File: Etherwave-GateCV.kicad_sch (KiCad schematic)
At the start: 32 parts

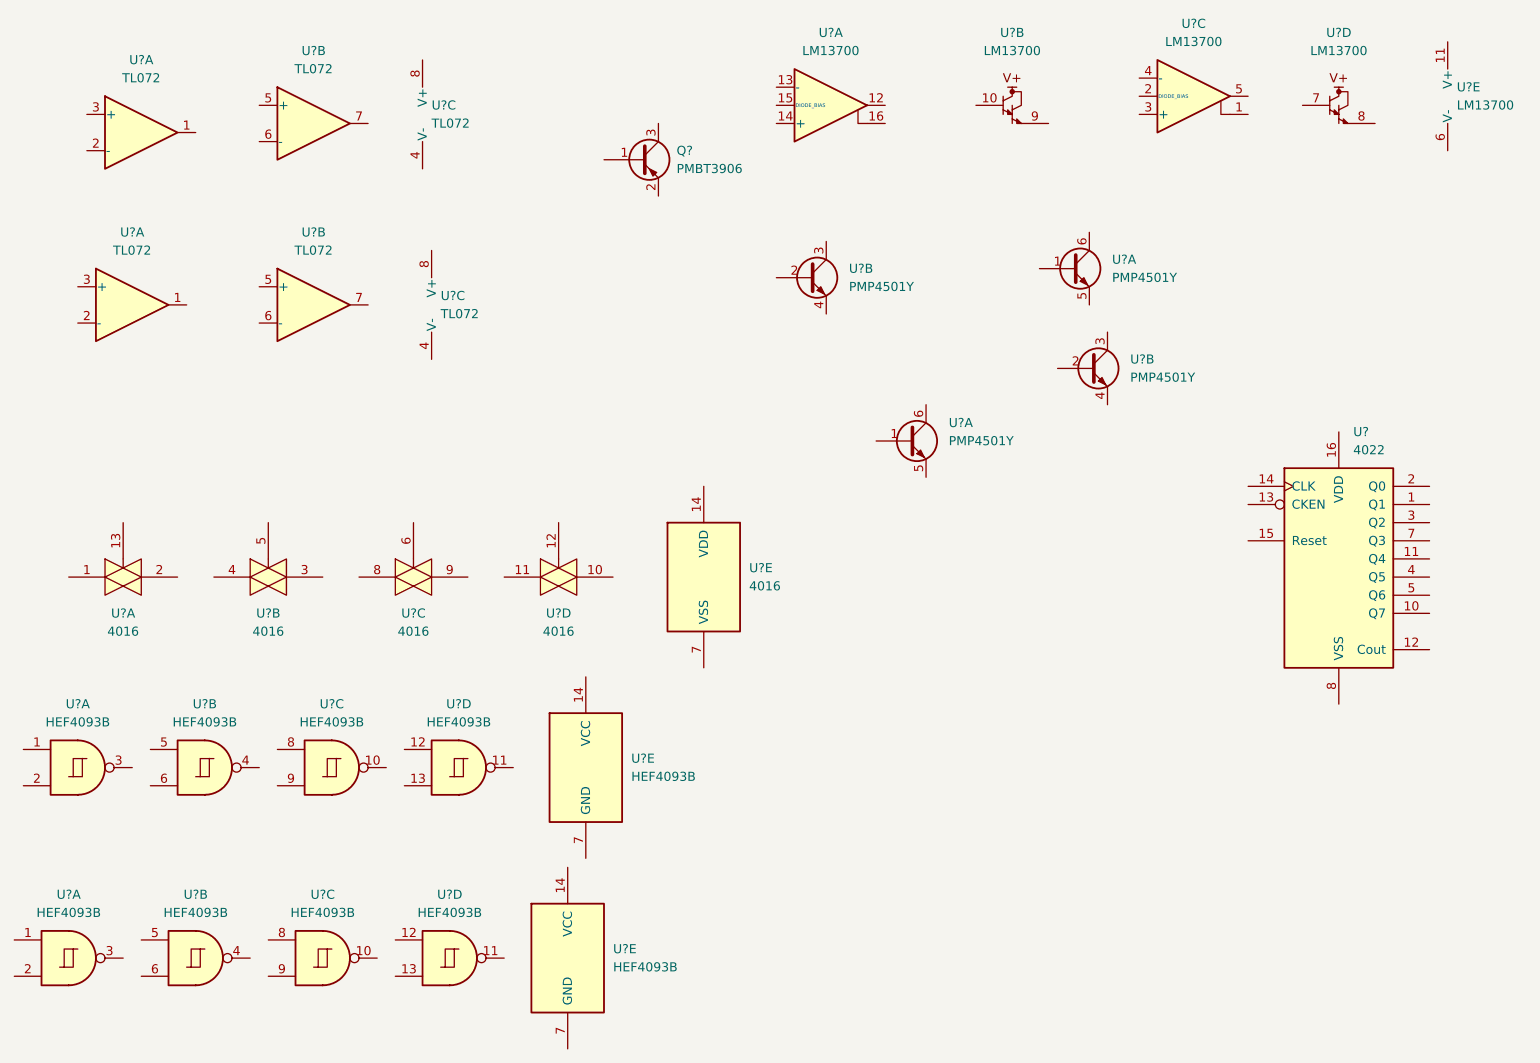
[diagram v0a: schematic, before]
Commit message: annotation for semiconductors
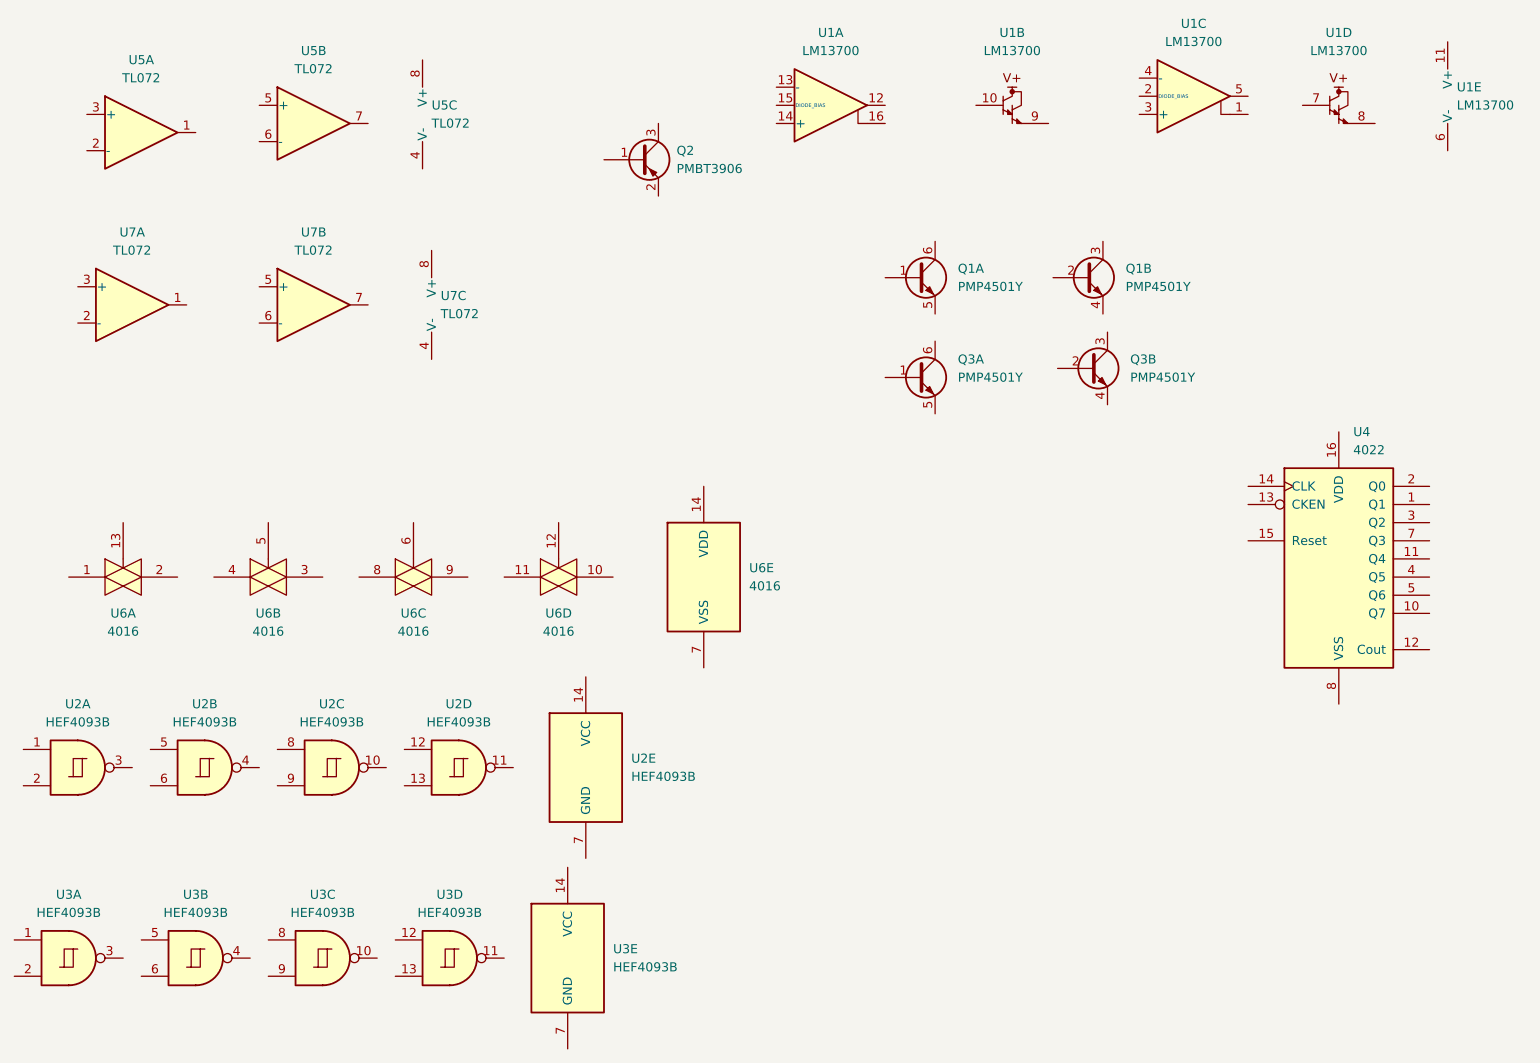
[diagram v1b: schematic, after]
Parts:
- gave numbers to parts that had none: 10
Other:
- moved on the sheet: Q1A, Q1B, Q3A

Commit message: footprint assignment for semiconductors
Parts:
- Q2: footprint Package_TO_SOT_SMD:SOT-23 -> Package_TO_SOT_SMD:SOT-23_Handsoldering
- U2, U3: footprint (none) -> Package_SO:TSSOP-14_4.4x5mm_P0.65mm
- U4: footprint (none) -> Package_SO:TSSOP-16_4.4x5mm_P0.65mm
- U6: footprint (none) -> Package_SO:SOIC-14_3.9x8.7mm_P1.27mm
- U7: footprint (none) -> Package_SO:SOIC-8_3.9x4.9mm_P1.27mm

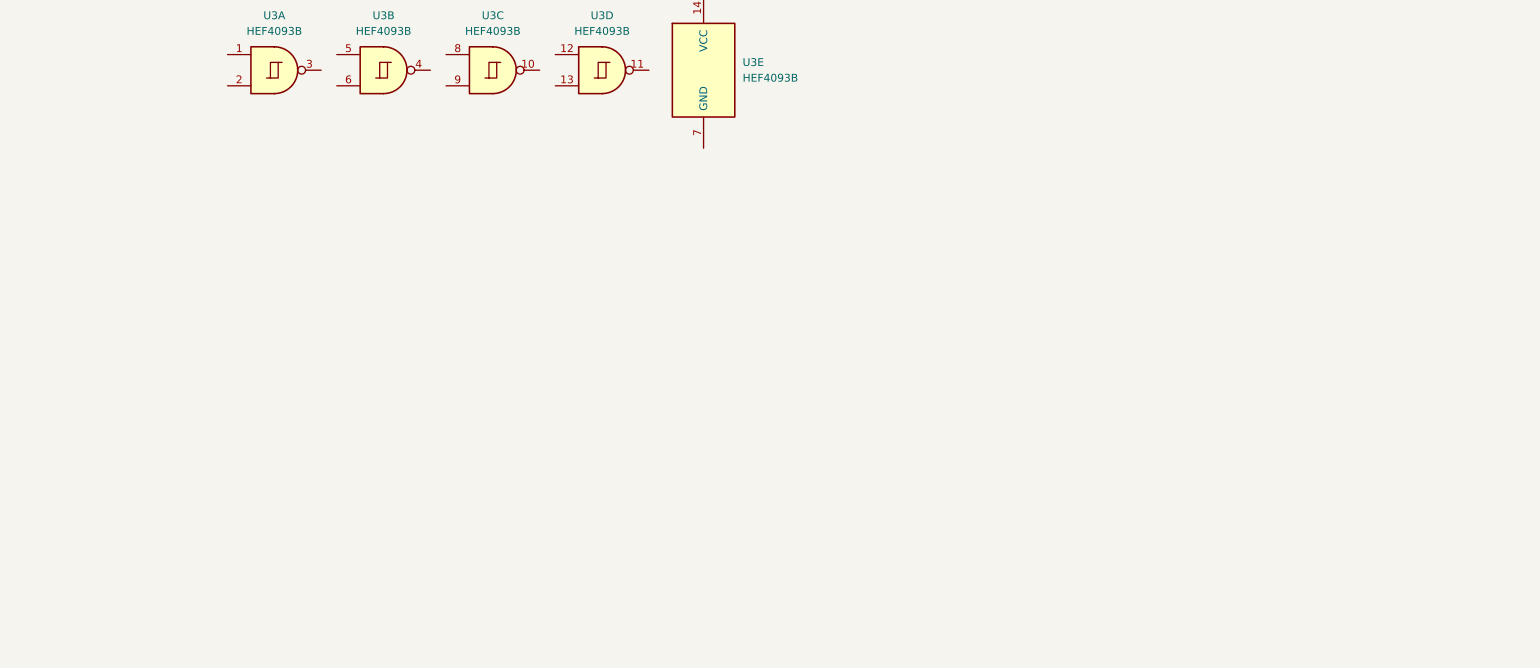
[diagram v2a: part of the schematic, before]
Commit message: placed Volume CV Circuit
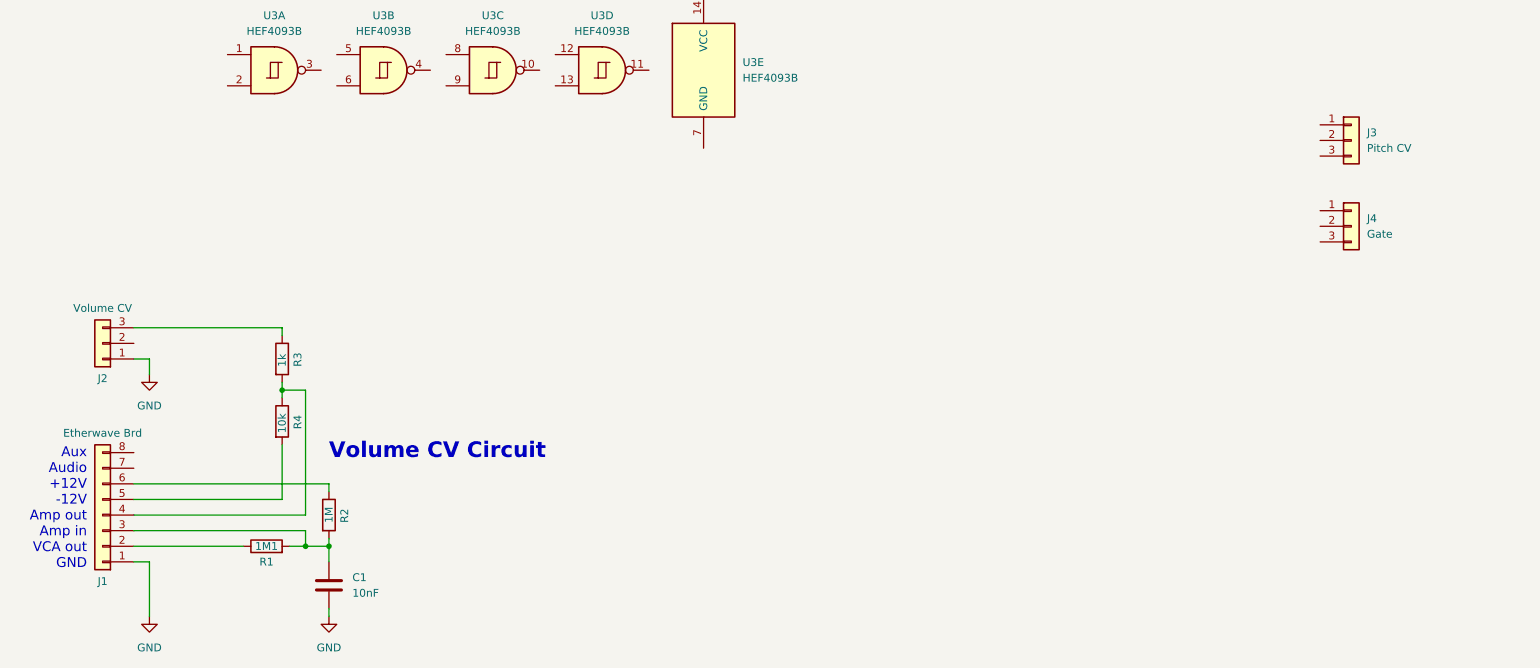
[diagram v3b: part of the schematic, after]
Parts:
- added C1: 10nF, symbol Device:C
- added J1: Etherwave Brd, symbol Connector_Generic:Conn_01x08
- added J2: Volume CV, symbol Connector_Generic:Conn_01x03
- added J3: Pitch CV, symbol Connector_Generic:Conn_01x03
- added J4: Gate, symbol Connector_Generic:Conn_01x03
- added R1: 1M1, symbol Device:R
- added R2: 1M, symbol Device:R
- added R3: 1k, symbol Device:R
- added R4: 10k, symbol Device:R
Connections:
- new net: J1.2 (Pin_2), R1.1
- new net: C1.1, J1.3 (Pin_3), R1.2, R2.2
- new net: J1.4 (Pin_4), R3.2, R4.1
- new net: J1.5 (Pin_5), R4.2
- new net: J1.6 (Pin_6), R2.1
- new net: J2.3 (Pin_3), R3.1
- new net GND: C1.2, J1.1 (Pin_1), J2.1 (Pin_1)
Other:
- note added: "Aux Audio +12V -12V Amp out Amp in VCA out GND"
- note added: "Volume CV Circuit"

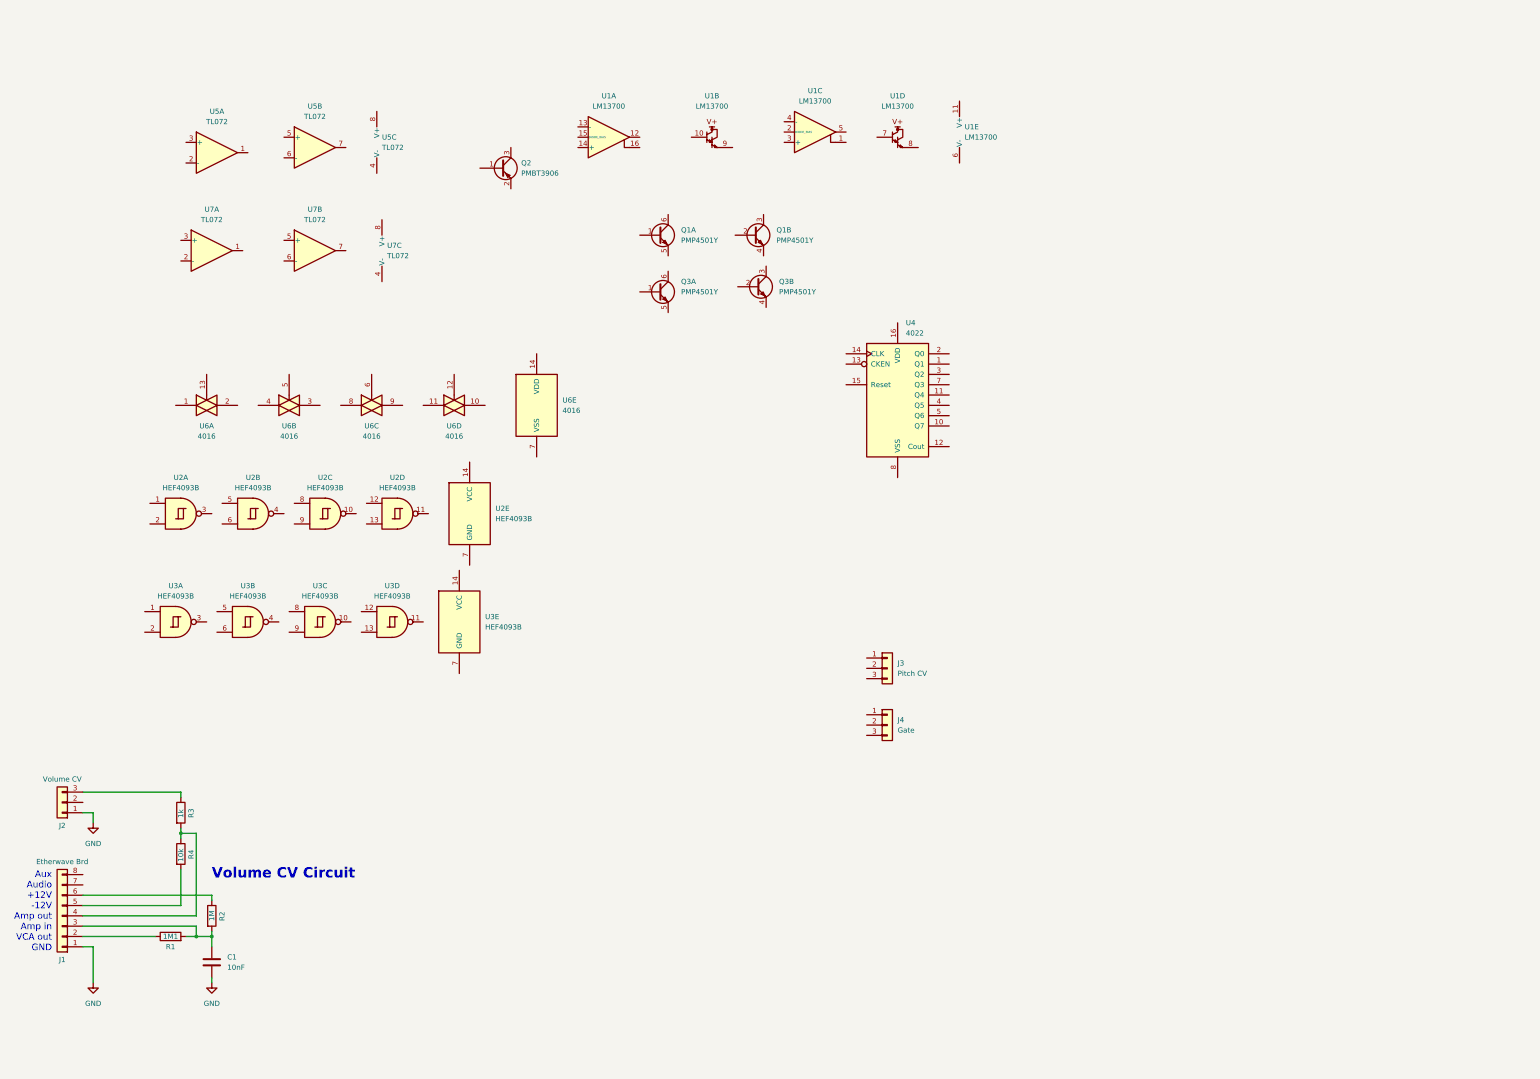
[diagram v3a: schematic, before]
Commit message: placed power section and started with circuit from Audio in
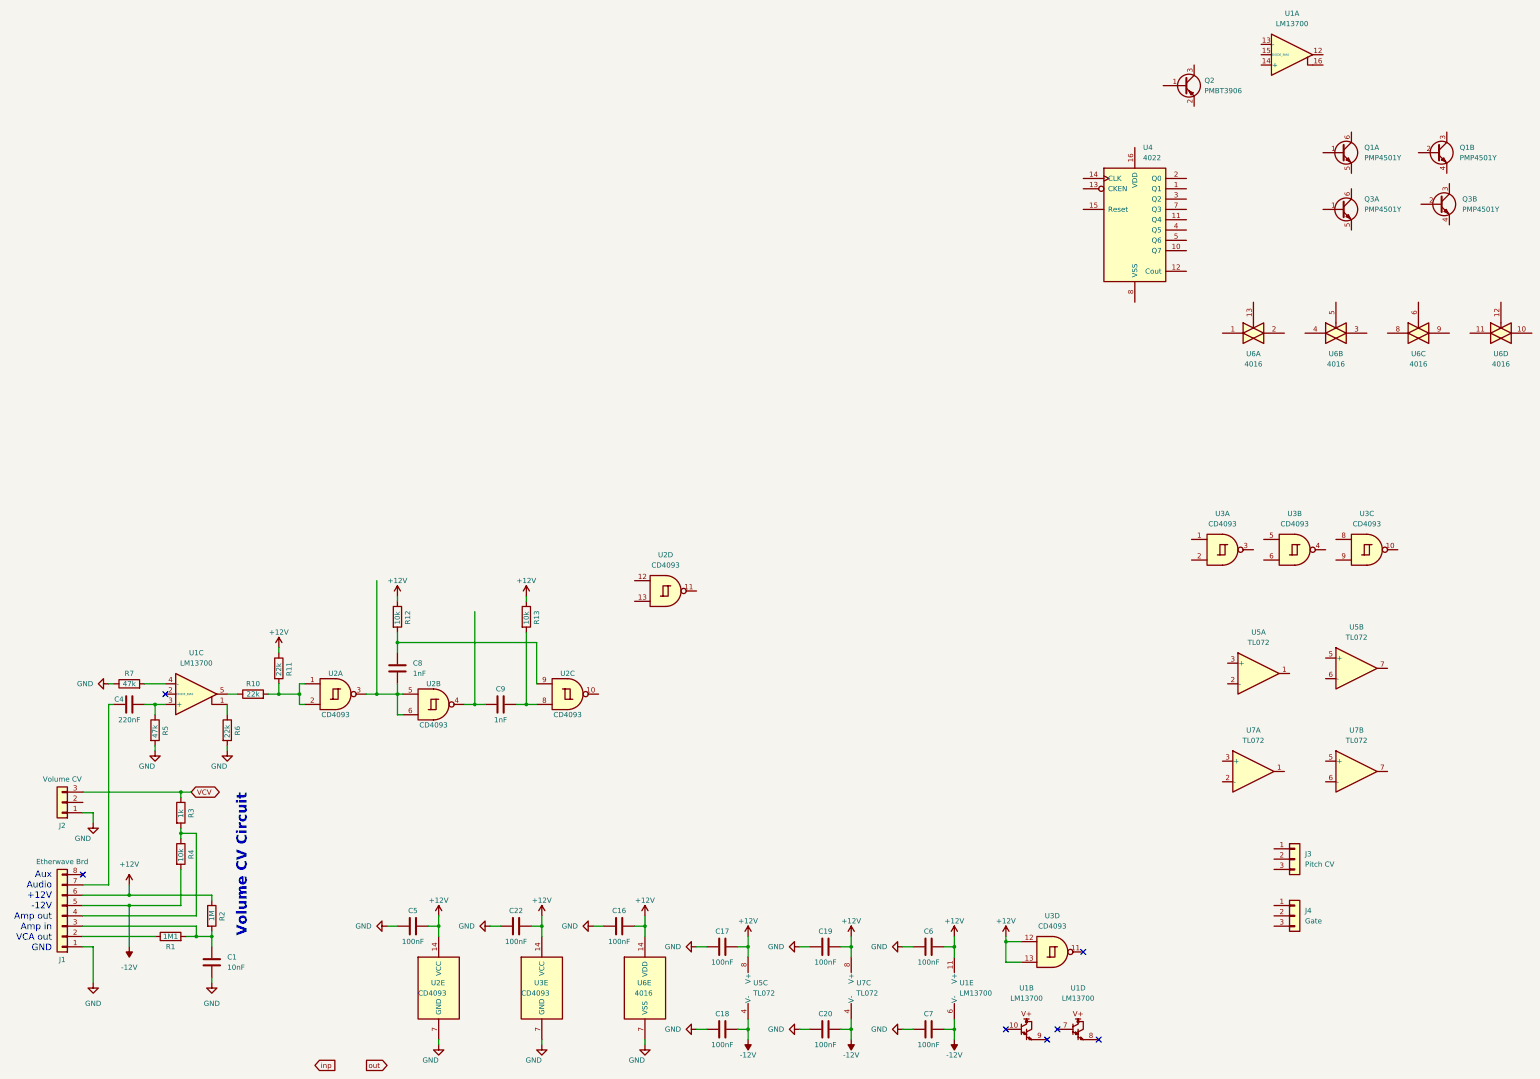
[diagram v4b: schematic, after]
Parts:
- added C16, C17, C18, C19, C20, C22, C5, C6, C7: 100nF, symbol Device:C
- added C4: 220nF, symbol Device:C
- added C8, C9: 1nF, symbol Device:C
- added R10, R11, R6: 22k, symbol Device:R
- added R12, R13: 10k, symbol Device:R
- added R5, R7: 47k, symbol Device:R
- U2, U3: value HEF4093B -> CD4093
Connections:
- net GND: now also U2.7 (GND), U3.7 (GND), U6.7 (VSS), C16.1, C17.1, C18.1, C19.1, C20.1, C22.1, C5.1, C6.1, C7.1, R5.2, R6.2, R7.1
- net +12V: now reaches U1.11 (V+)
- net +12V: now also J1.6 (Pin_6), R2.1, U2.14 (VCC), U3.12, U3.13, U3.14 (VCC), U5.8 (V+), U6.14 (VDD), U7.8 (V+), C16.2, C17.2, C19.2, C22.2, C5.2, C6.2, R11.1, R12.1, R13.1
- net -12V: now reaches U1.6 (V-)
- net -12V: now also J1.5 (Pin_5), R4.2, U5.4 (V-), U7.4 (V-), C18.2, C20.2, C7.2
- net at J1.7 (Pin_7): now also C4.1
- net at U2.4: now also C9.1
- net at U2.5: now also U2.3, U2.6, C8.2
- net at U2.8: now also C9.2, R13.2
- net at U2.9: now also C8.1, R12.2
- net VCV: now reaches J2.3 (Pin_3), R3.1
- net at U2.1: now also U2.2, R10.2, R11.2
- net at U1.1: now also R6.1
- net at U1.3 (+): now also C4.2, R5.1
- net at U1.4 (-): now also R7.2
- net at U1.5: now also R10.1
- no-connect marks 0 -> 7
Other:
- moved on the sheet: J3, J4, Q1A, Q1B, Q2, Q3A, Q3B, U1A, U1B, U1C, U1D, U1E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
